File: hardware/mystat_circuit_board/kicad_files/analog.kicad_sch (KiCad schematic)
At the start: 46 parts, among them J4 Screw_Terminal_01x04, K1 9011-05-11, K2 9011-05-11, K3 9011-05-11, K4 9011-05-11, K5 9011-05-11, U10 OPA192, U11 BUF634AIDDAR, U12 ADG1419, U13 OPA192, U14 OPA192, U15 OPA192, U16 OPA192, U17 OPA192

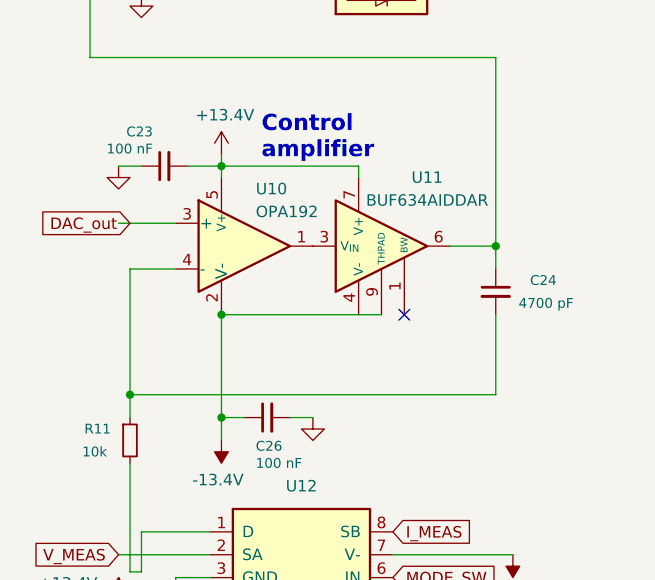
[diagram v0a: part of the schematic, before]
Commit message: change micro USB to USB C 16P 2.0, rotate U11 for routing of thermal pad version
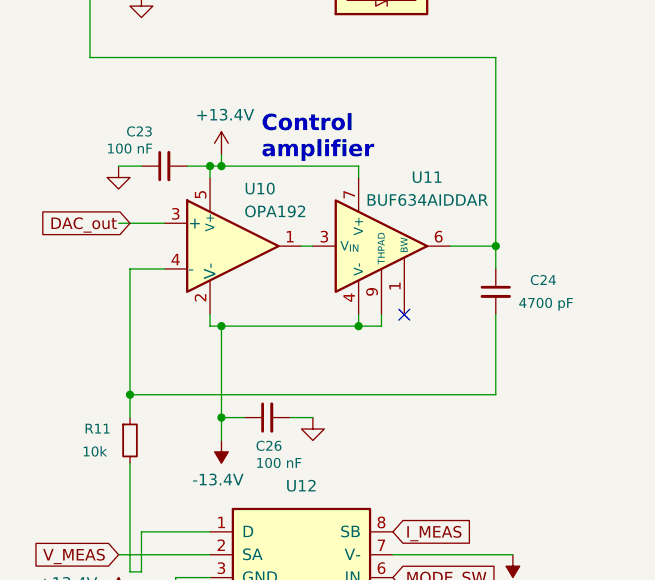
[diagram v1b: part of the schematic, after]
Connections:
- net -13.4V: now also U11.4 (V-)
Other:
- moved on the sheet: U10

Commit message: partway through adding normal reed relay size
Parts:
- removed K1, K2, K3, K4, K5: 9011-05-11, my_footprints:relay_9011-05-11, symbol mylib:9011-05-11
- added K1, K2, K3, K4, K5: (no value), my_footprints:Reed_Relay_MiRelay_SIP-HV1A05D, symbol mylib:SIP-HV1A05D
- J4: footprint (none) -> TerminalBlock_Phoenix:TerminalBlock_Phoenix_MPT-0,5-4-2.54_1x04_P2.54mm_Horizontal
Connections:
- net CELL_ON: now also K1.3
- net GND: now also K1.2, K2.1, K2.2, K3.1, K3.2, K4.1, K4.2, K5.1, K5.2
- net RANGE1: now also K5.3
- net RANGE2: now also K4.3
- net RANGE3: now also K3.3
- net RANGE4: now also K2.3
- net WE: now also K1.1
- net at C24.1, R10.1, U11.6: now also K1.4
- net at R24.2: now also K4.4
- net at R19.2: now also K3.4
- net at R16.2: now also K2.4
- net at R25.2: now also K5.4
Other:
- moved on the sheet: C25, R10, R16, R19, R24, R25

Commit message: more pcb layout progress save
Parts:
- C23, C25, C26, C27, C28, C29, C30, C31, C32, C34, C35, C36, C37: MPN (none) -> 08055C104KAT2A
- C24: MPN (none) -> CC0805KRX7R9BB472
- C33, C38: MPN (none) -> CC0805JRNPO9BN120
- J4: footprint TerminalBlock_Phoenix:TerminalBlock_Phoenix_MPT-0,5-4-2.54_1x04_P2.54mm_Horizontal -> easyeda2kicad:CONN-TH_4P-P2.54_MX128-2.54-GN01-04P-CU-Y-A; LCSC Part (none) -> C5188444; MPN (none) -> MX128-2.54-04P-GN01-Cu-Y-A; Part Number (none) -> MX128-2.54-04P-GN01-Cu-Y-A
- K1, K2, K3, K4, K5: LCSC C41371794 -> (none); LCSC Part (none) -> C41371794; MPN (none) -> SIP-HV1A05D
- R10: MPN (none) -> ERJ-6ENF27R0V
- R11: MPN (none) -> RC0805FR-0710KL
- R12, R14: MPN (none) -> ERA-6AEB4023V
- R13, R15, R17, R18, R20, R22: MPN (none) -> ERA-6AEB753V
- R16: MPN (none) -> ERA-6AEB104V
- R19: MPN (none) -> ERA-6AEB102V
- R21: MPN (none) -> ERA-6AEB183V
- R23: MPN (none) -> ERA-6AEB202V
- R24: MPN (none) -> 2-1625868-7
- R25: MPN (none) -> RT0805BRD071RL; Manufacturer Susumu -> YAGEO; Part Number RL1220S-1R0-F -> RT0805BRD071RL
- U10, U13, U14, U15, U16, U17: MPN (none) -> OPA192IDBVR
- U11: symbol Amplifier_Buffer:BUF634AxDDA -> mylib:BUF634AxDDA
- U12: MPN (none) -> ADG1419BRMZ-REEL7

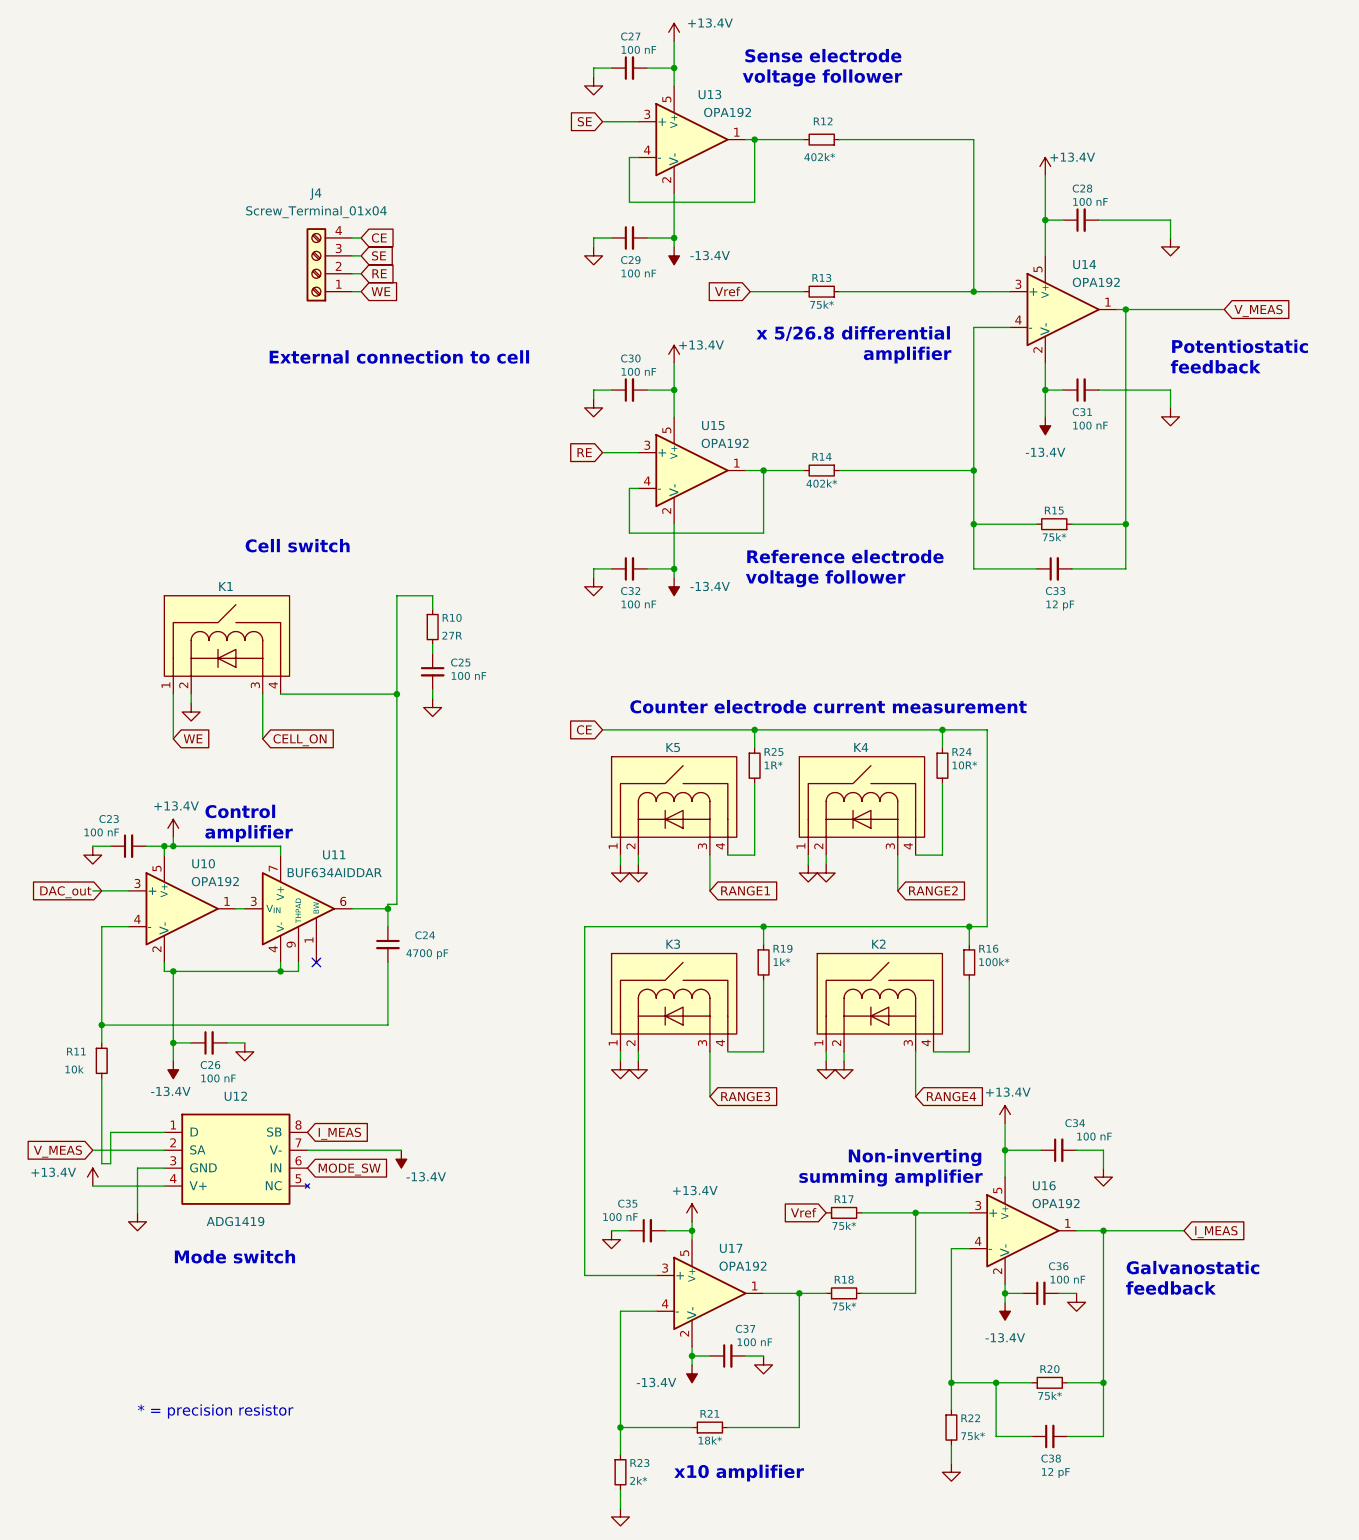
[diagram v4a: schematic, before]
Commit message: change relays back to original tdstat, re-add GND connection, add changelog from now on
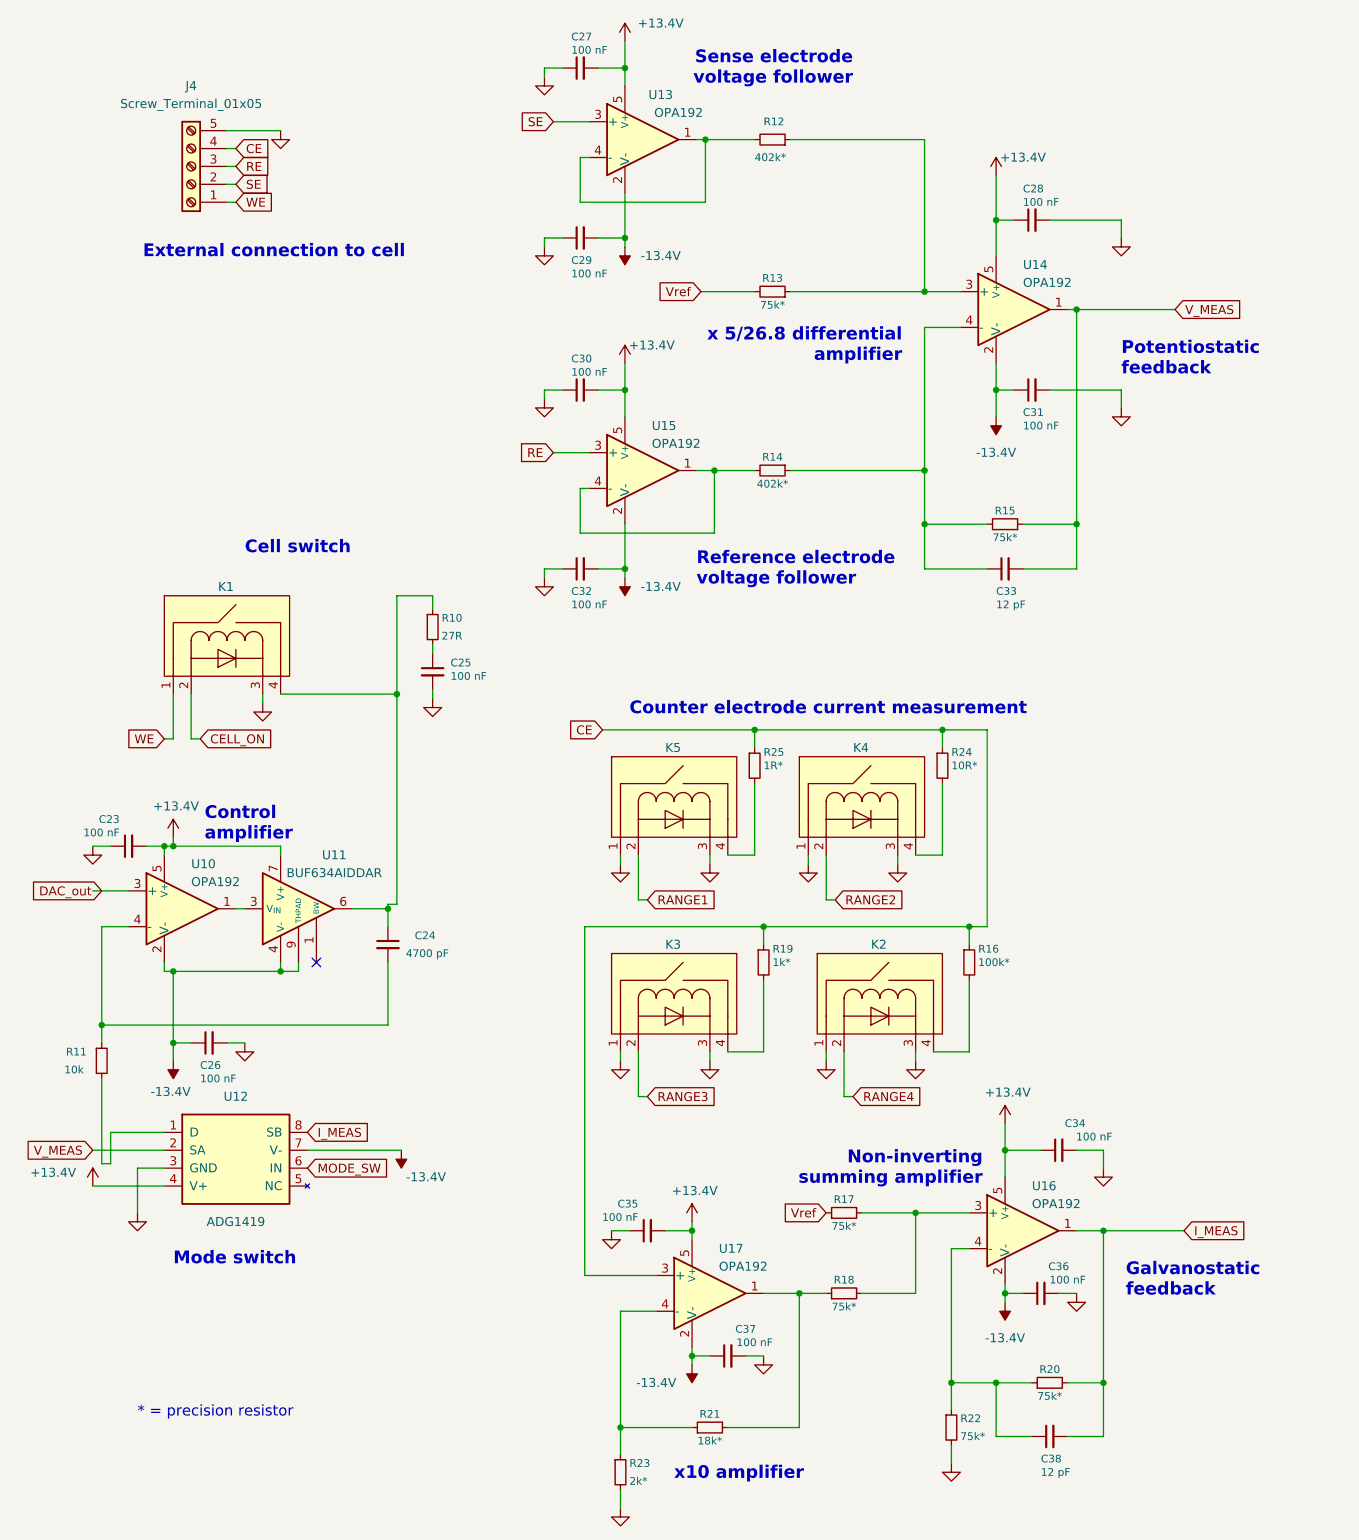
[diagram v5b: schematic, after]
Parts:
- J4: value Screw_Terminal_01x04 -> Screw_Terminal_01x05; footprint easyeda2kicad:CONN-TH_4P-P2.54_MX128-2.54-GN01-04P-CU-Y-A -> easyeda2kicad:CONN-TH_5P-P2.54_MX128-2.54-05P-GN01-CU-Y-A; symbol Connector:Screw_Terminal_01x04 -> Connector:Screw_Terminal_01x05; LCSC Part C5188444 -> C5188445; MPN MX128-2.54-04P-GN01-Cu-Y-A -> MX128-2.54-05P-GN01-Cu-Y-A
- K1, K2, K3, K4, K5: footprint my_footprints:Reed_Relay_MiRelay_SIP-HV1A05D -> easyeda2kicad:SIP-4_L19.6-W5.4-P5.08_9007-SPST-NO; symbol mylib:SIP-HV1A05D -> mylib:9007-05-01_2026; LCSC Part C41371794 -> C6111158; MPN SIP-HV1A05D -> 9007-05-01; Manufacturer MiRelay -> COTO
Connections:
- net CELL_ON: now also K1.2; no longer K1.3
- net GND: now also J4.5 (Pin_5), K1.3, K2.3, K3.3, K4.3, K5.3; no longer K1.2, K2.2, K3.2, K4.2, K5.2
- net RANGE1: now also K5.2; no longer K5.3
- net RANGE2: now also K4.2; no longer K4.3
- net RANGE3: now also K3.2; no longer K3.3
- net RANGE4: now also K2.2; no longer K2.3
- net RE: now also J4.3 (Pin_3); no longer J4.2 (Pin_2)
- net SE: now also J4.2 (Pin_2); no longer J4.3 (Pin_3)
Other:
- moved on the sheet: C27, C28, C29, C30, C31, C32, C33, R12, R13, R14, R15, U13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

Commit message: mostly resistor changes
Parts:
- C23, C25, C26, C27, C28, C29, C30, C31, C32, C34, C35, C36, C37: LCSC Part (none) -> C49678; MPN 08055C104KAT2A -> CC0805KRX7R9BB104; Manufacturer AVX Corporation -> YAGEO; Part Number 08055C104KAT2A -> (none)
- C24: value 4700 pF -> 4.7 nF; LCSC Part (none) -> C107153; Part Number CC0805KRX7R9BB472 -> (none)
- C33, C38: footprint Capacitor_SMD:C_0805_2012Metric -> Capacitor_SMD:C_0603_1608Metric; LCSC Part (none) -> C38523; MPN CC0805JRNPO9BN120 -> CL10C120JB8NNNC; Manufacturer Yageo -> Samsung Electro-Mechanics; Part Number CC0805JRNPO9BN120 -> (none)
- J3: renamed from J4; Part Number MX128-2.54-04P-GN01-Cu-Y-A -> (none)
- K1, K2, K3, K4, K5: Part Number SIP-HV1A05D -> (none); now not fitted
- R10: LCSC Part (none) -> C17594; MPN ERJ-6ENF27R0V -> 0805W8F270JT5E; Manufacturer Panasonic Electronic Components -> UNI-ROYAL; Part Number ERJ-6ENF27R0V -> (none)
- R11: LCSC Part (none) -> C84376; Part Number RC0805FR-0710KL -> (none)
- R12, R14: LCSC Part (none) -> C425384; MPN ERA-6AEB4023V -> TC0525B4023T5E; Manufacturer Panasonic Electronic Components -> UNI-ROYAL; Part Number ERA-6AEB4023V -> (none)
- R13, R15, R17, R18, R20, R22: LCSC Part (none) -> C473313; Part Number ERA-6AEB753V -> (none)
- R16: LCSC Part (none) -> C192074; Part Number ERA-6AEB104V -> (none)
- R19: LCSC Part (none) -> C192073; Part Number ERA-6AEB102V -> (none)
- R21: LCSC Part (none) -> C473303; Part Number ERA-6AEB183V -> (none)
- R23: LCSC Part (none) -> C417117; Part Number ERA-6AEB202V -> (none)
- R24: footprint Resistor_SMD:R_0805_2012Metric -> Resistor_SMD:R_1206_3216Metric; LCSC Part (none) -> C309661; MPN 2-1625868-7 -> RT1206BRD0710RL; Manufacturer TE Connectivity Passive Product -> YAGEO; Part Number 2-1625868-7 -> (none)
- R25: footprint Resistor_SMD:R_0805_2012Metric -> Resistor_SMD:R_1206_3216Metric; LCSC Part (none) -> C513714; MPN RT0805BRD071RL -> RT1206BRD071RL; Part Number RT0805BRD071RL -> (none)
- U10, U13, U14, U15, U16, U17: LCSC Part (none) -> C139648; Part Number OPA192IDBVR -> (none)
- U11: LCSC Part (none) -> C2864582; MPN (none) -> BUF634AIDDAR; Manufacturer (none) -> Texas Instruments
- U12: LCSC Part (none) -> C459694; MPN ADG1419BRMZ-REEL7 -> ADG1419BRMZ; Part Number ADG1419BRMZ-REEL7 -> (none)

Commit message: resistor change
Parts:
- R16: LCSC Part C192074 -> C3034987; MPN ERA-6AEB104V -> TNPW0805100KBEEA; Manufacturer Panasonic Electronic Components -> VISHAY
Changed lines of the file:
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@@
 			)
 		)
-		(property "Datasheet" "https://industrial.panasonic.com/cdbs/www-data/pdf/RDM0000/AOA0000C307.pdf"
+		(property "Datasheet" ""
 			(at 156.21 149.86 0)
 			(hide yes)
@@
 			)
 		)
-		(property "Manufacturer" "Panasonic Electronic Components"
+		(property "Manufacturer" "VISHAY"
 			(at 156.21 149.86 0)
 			(hide yes)
@@
 			)
 		)
-		(property "MPN" "ERA-6AEB104V"
+		(property "MPN" "TNPW0805100KBEEA"
 			(at 156.21 149.86 0)
 			(hide yes)
@@
 			)
 		)
-		(property "LCSC Part" "C192074"
+		(property "LCSC Part" "C3034987"
 			(at 156.21 149.86 0)
 			(hide yes)
